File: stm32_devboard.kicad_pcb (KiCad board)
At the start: 2 copper layers, 21.6 x 50.2 mm, 30 parts, among them SW1 Reset, SW2 User_Press, U1 XC6206P332MR-G, U2 STM32F072CBT6, Y1 8MHz

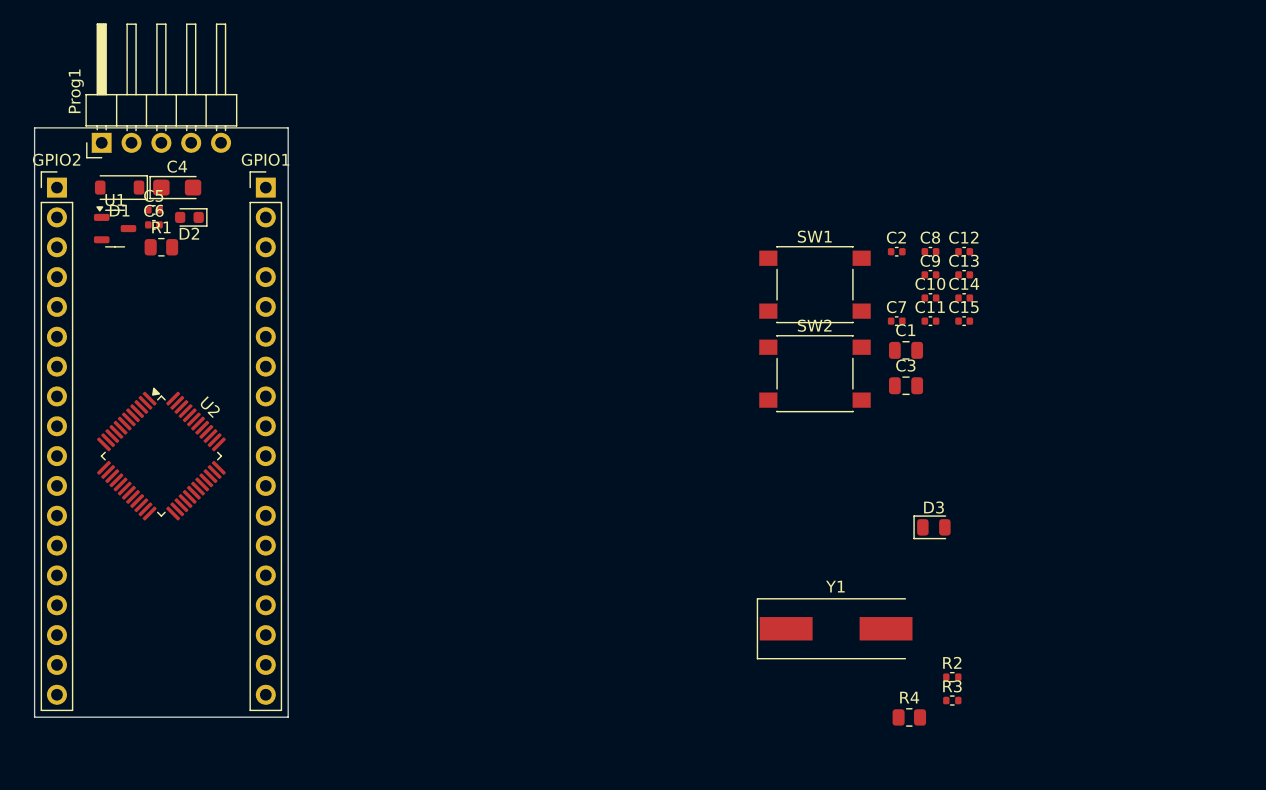
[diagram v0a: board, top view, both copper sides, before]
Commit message: update pcb from schem
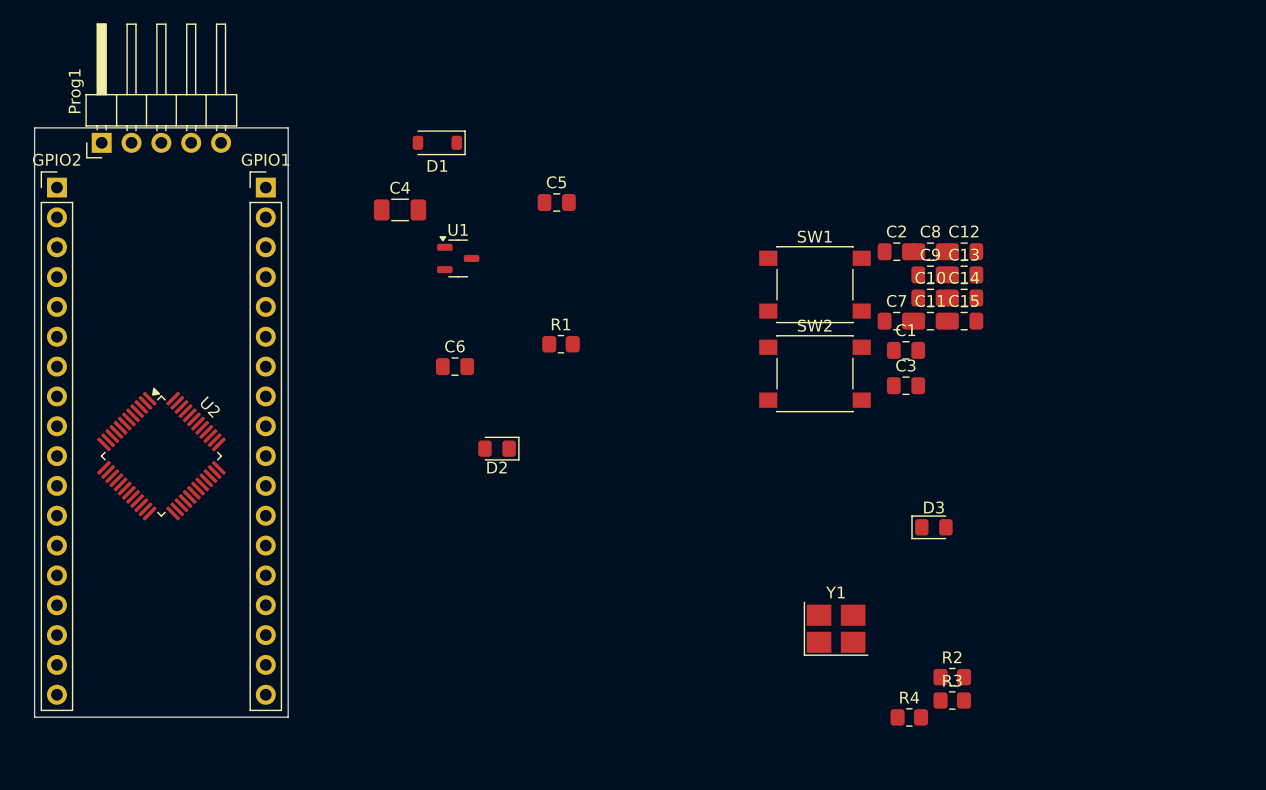
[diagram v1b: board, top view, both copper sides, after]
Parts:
- C1, C3: footprint Capacitor_SMD:C_0805_2012Metric -> Capacitor_SMD:C_0805_2012Metric_Pad1.18x1.45mm_HandSolder
- C10, C11, C12, C13, C14, C15, C2, C5, C6, C7, C8, C9: footprint Capacitor_SMD:C_0402_1005Metric -> Capacitor_SMD:C_0805_2012Metric_Pad1.18x1.45mm_HandSolder
- C4: footprint Capacitor_Tantalum_SMD:CP_EIA-3216-18_Kemet-A -> Capacitor_SMD:C_1206_3216Metric_Pad1.33x1.80mm_HandSolder
- D2: footprint LED_SMD:LED_0603_1608Metric -> LED_SMD:LED_0805_2012Metric_Pad1.15x1.40mm_HandSolder
- D3: footprint LED_SMD:LED_0805_2012Metric -> LED_SMD:LED_0805_2012Metric_Pad1.15x1.40mm_HandSolder
- R1, R4: footprint Resistor_SMD:R_0805_2012Metric -> Resistor_SMD:R_0805_2012Metric_Pad1.20x1.40mm_HandSolder
- R2, R3: footprint Resistor_SMD:R_0402_1005Metric -> Resistor_SMD:R_0805_2012Metric_Pad1.20x1.40mm_HandSolder
- U1: value XC6206P332MR-G -> AP2210-3.3
- Y1: footprint Crystal:Crystal_SMD_HC49-SD -> Crystal:Crystal_SMD_3225-4Pin_3.2x2.5mm_HandSoldering
- moved R1 35.0 mm to (95.0, 87.0)
- moved C5 34.3 mm to (94.6, 74.9)
- moved D2 32.8 mm to (89.5, 95.9)
- moved U1 29.3 mm to (86.2, 79.7)
- moved C6 28.3 mm to (86.0, 88.9)
- moved D1 27.3 mm to (84.5, 69.8)
- moved C4 19.1 mm to (81.3, 75.6)

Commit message: pcb work
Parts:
- moved R4 78.8 mm to (57.1, 78.0), turned to -90 degrees
- moved D3 75.8 mm to (56.1, 74.9), turned to 180 degrees
- moved R2 73.5 mm to (54.9, 113.6), turned to -90 degrees
- moved C9 71.0 mm to (55.9, 89.2)
- moved C10 70.7 mm to (55.9, 87.1)
- moved C13 69.1 mm to (64.0, 103.6), turned to 180 degrees
- moved Y1 67.4 mm to (57.4, 82.6)
- moved C2 61.5 mm to (62.3, 83.9), turned to 180 degrees
- moved SW1 61.4 mm to (61.0, 108.0), turned to 180 degrees
- moved R3 61.4 mm to (67.1, 113.5), turned to 90 degrees
- moved SW2 61.2 mm to (61.0, 114.9), turned to 180 degrees
- moved R1 40.9 mm to (55.1, 78.0), turned to 90 degrees
- moved D2 40.5 mm to (56.1, 72.9)
- moved C5 30.0 mm to (64.8, 78.0)
- moved C6 28.8 mm to (59.5, 77.5), turned to -90 degrees
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
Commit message: PCB rev 1
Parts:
- moved C10 88.9 mm to (144.8, 87.2)
- moved C9 88.9 mm to (144.8, 89.3)
- moved R1 82.6 mm to (137.7, 81.5)
- moved R4 82.6 mm to (139.7, 81.2)
- moved C6 82.3 mm to (141.7, 81.3)
- moved C2 82.1 mm to (141.0, 107.4), turned to 0 degrees
- moved C13 80.9 mm to (144.8, 107.4)
- moved Y1 80.7 mm to (138.0, 85.7)
- moved GPIO1 80.1 mm to (149.9, 77.5)
- moved GPIO2 80.1 mm to (132.1, 77.5)
- moved D1 80.1 mm to (145.3, 77.0)
- moved C4 80.1 mm to (145.4, 79.5)
- moved C5 80.1 mm to (144.8, 81.8)
- moved Prog1 80.1 mm to (135.9, 73.7)
- moved R2 80.1 mm to (134.9, 117.4)
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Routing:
- net GND: track 0.00 -> 105.4 mm, vias 0 -> 12
- net +3.3V: track 0.00 -> 76.4 mm, vias 0 -> 5
- net /NRST: track 0.00 -> 47.2 mm, vias 0 -> 3
- net /USER_LED: track 0.00 -> 36.1 mm, vias 0 -> 4
- net /SWCLK: track 0.00 -> 34.1 mm, vias 0 -> 2
- net /SWDIO: track 0.00 -> 27.0 mm, vias 0 -> 1
- net /PB13: track 0.00 -> 26.0 mm, vias 0 -> 2
- net /PB12: track 0.00 -> 25.5 mm, vias 0 -> 2
- net /PB11: track 0.00 -> 23.7 mm, vias 0 -> 1
- net /PB14: track 0.00 -> 22.7 mm, vias 0 -> 2
- net /USER_BTN: track 0.00 -> 21.3 mm
- net /PB10: track 0.00 -> 21.1 mm, vias 0 -> 2
- net /PB2: track 0.00 -> 18.7 mm, vias 0 -> 2
- net /PB15: track 0.00 -> 16.8 mm, vias 0 -> 2
- net /PB9: track 0.00 -> 16.8 mm
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- added copper zone on F.Cu, net GND
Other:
- board size 21.6 x 50.2 mm -> 21.6 x 50.4 mm

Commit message: rev1
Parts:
- added G***: LOGO, LOGO, F.Cu at (132.5, 74.1)
- Y1: footprint Crystal:Crystal_SMD_3225-4Pin_3.2x2.5mm_HandSoldering -> Crystal:Crystal_SMD_Abracon_ABM3-2Pin_5.0x3.2mm_HandSoldering
- moved C10 1.61 mm to (145.3, 85.7)
- moved C9 1.61 mm to (145.3, 87.8)
- moved C12 1.47 mm to (137.2, 103.9)
- moved C8 1.47 mm to (137.2, 106.0)
- moved Y1 0.79 mm to (138.7, 86.2), turned to 180 degrees
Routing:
- net GND: track 105.4 -> 116.0 mm
- net /HSE_IN: track 7.07 -> 9.93 mm
- net /PB10: track 21.1 -> 23.7 mm
- net /SWCLK: track 34.1 -> 36.5 mm, vias 2 -> 0
- net /PB11: track 23.7 -> 25.9 mm, vias 1 -> 2
- net /NRST: track 47.2 -> 49.1 mm
- net /PB9: track 16.8 -> 15.9 mm
- net /HSE_OUT: track 7.82 -> 7.87 mm, vias 2 -> 0
- net /PB2: vias 2 -> 0
- net /PB1: vias 2 -> 0
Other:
- board text added: "GND"
- board text added: "NRST"
- board text added: "Rev. 1"
- board text added: "SWCLK"
- board text added: "SWDIO"
- board text added: "VPP"
